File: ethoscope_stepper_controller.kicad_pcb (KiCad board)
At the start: 2 copper layers, 74.9 x 74.9 mm, 63 parts, among them P1 PWR_JACK_2.1x5.5_SMD_VERT, T1 TERM_BLK_HDR_4POS_VERT_0.138IN, T2 TERM_BLK_HDR_4POS_VERT_0.138IN, T3 TERM_BLK_HDR_4POS_VERT_0.138IN, T4 TERM_BLK_HDR_4POS_VERT_0.138IN, T5 TERM_BLK_HDR_4POS_VERT_0.138IN, T6 TERM_BLK_HDR_4POS_VERT_0.138IN, T7 TERM_BLK_HDR_4POS_VERT_0.138IN, U1 TMC429, U10 DRV8846, U2 DRV8846, U3 DRV8846, U4 DRV8846, U5 TMC429, U6 DRV8846, U7 DRV8846, U8 DRV8846, U9 TMC429

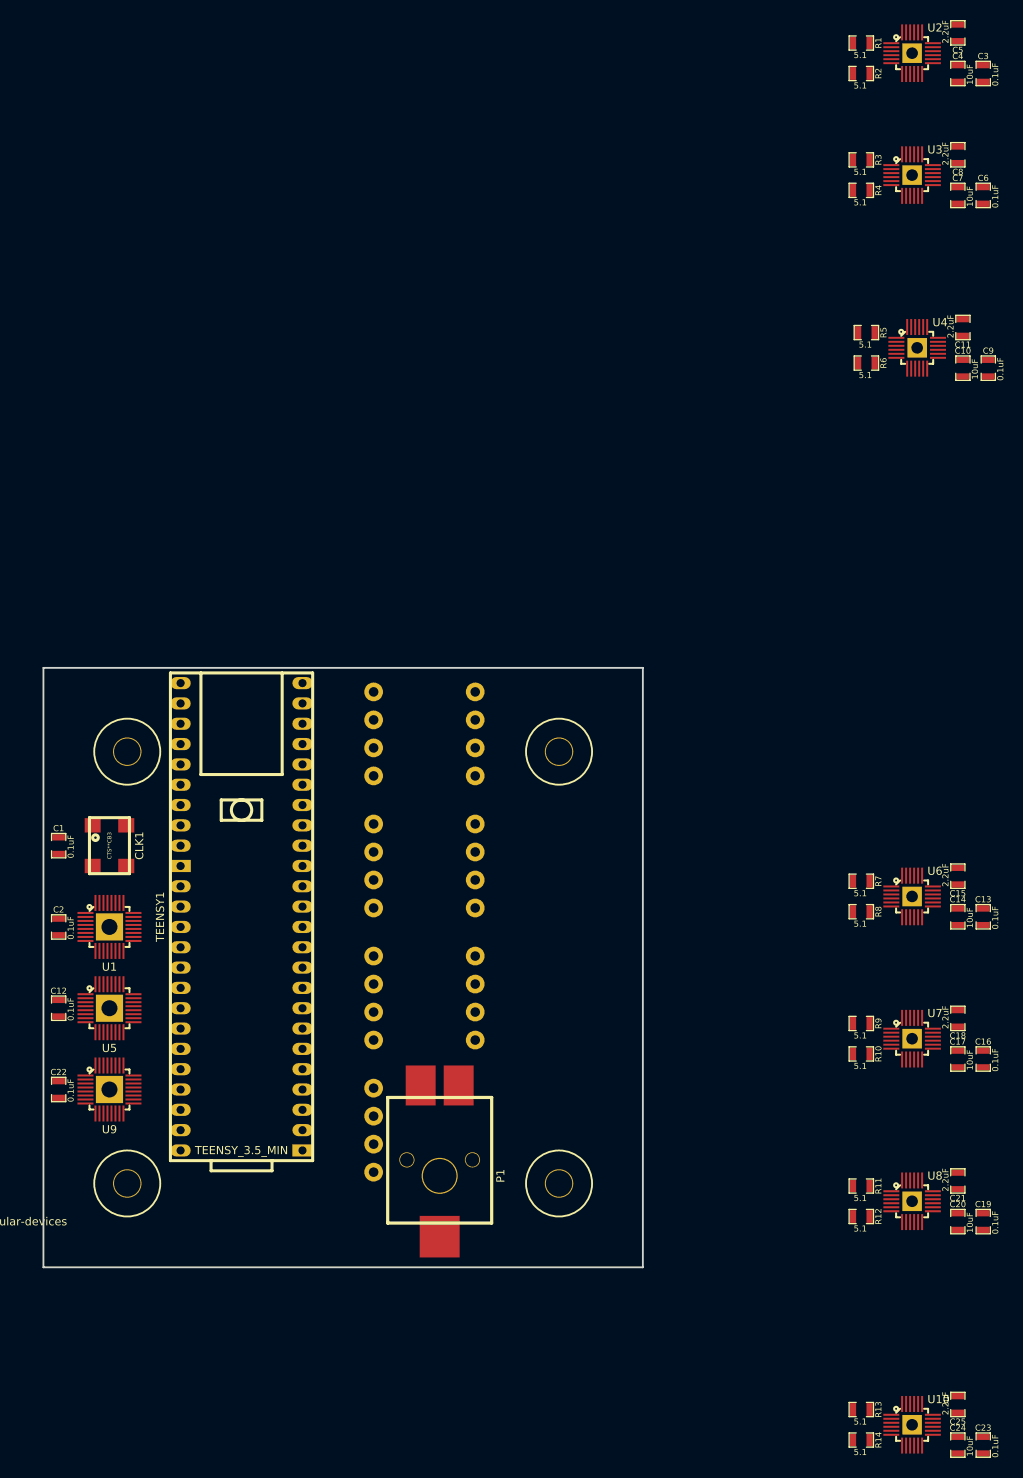
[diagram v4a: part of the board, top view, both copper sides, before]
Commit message: Added a pull-up resistor and tri-state buffer.
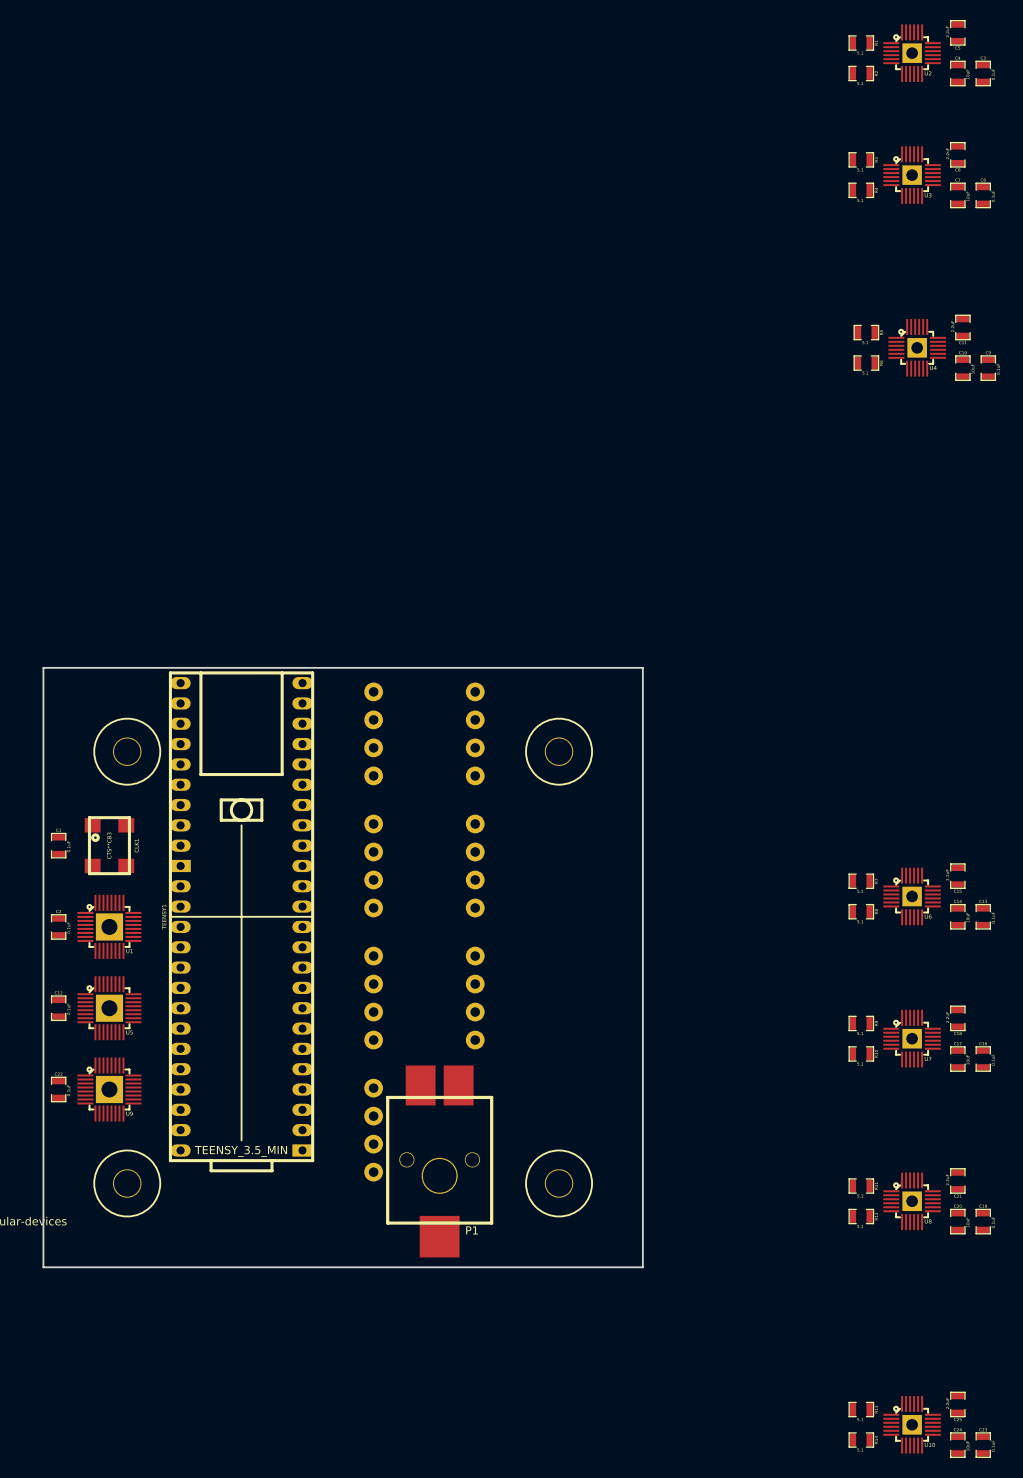
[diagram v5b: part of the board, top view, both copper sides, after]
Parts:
- C10, C11, C14, C15, C17, C18, C20, C21, C24, C25, C4, C5, C7, C8, R1, R10, R11, R12, R13, R14, R2, R3, R4, R5, R6, R7, R8, R9: footprint footprints:SM0805 -> ethoscope_stepper_controller:SM0805

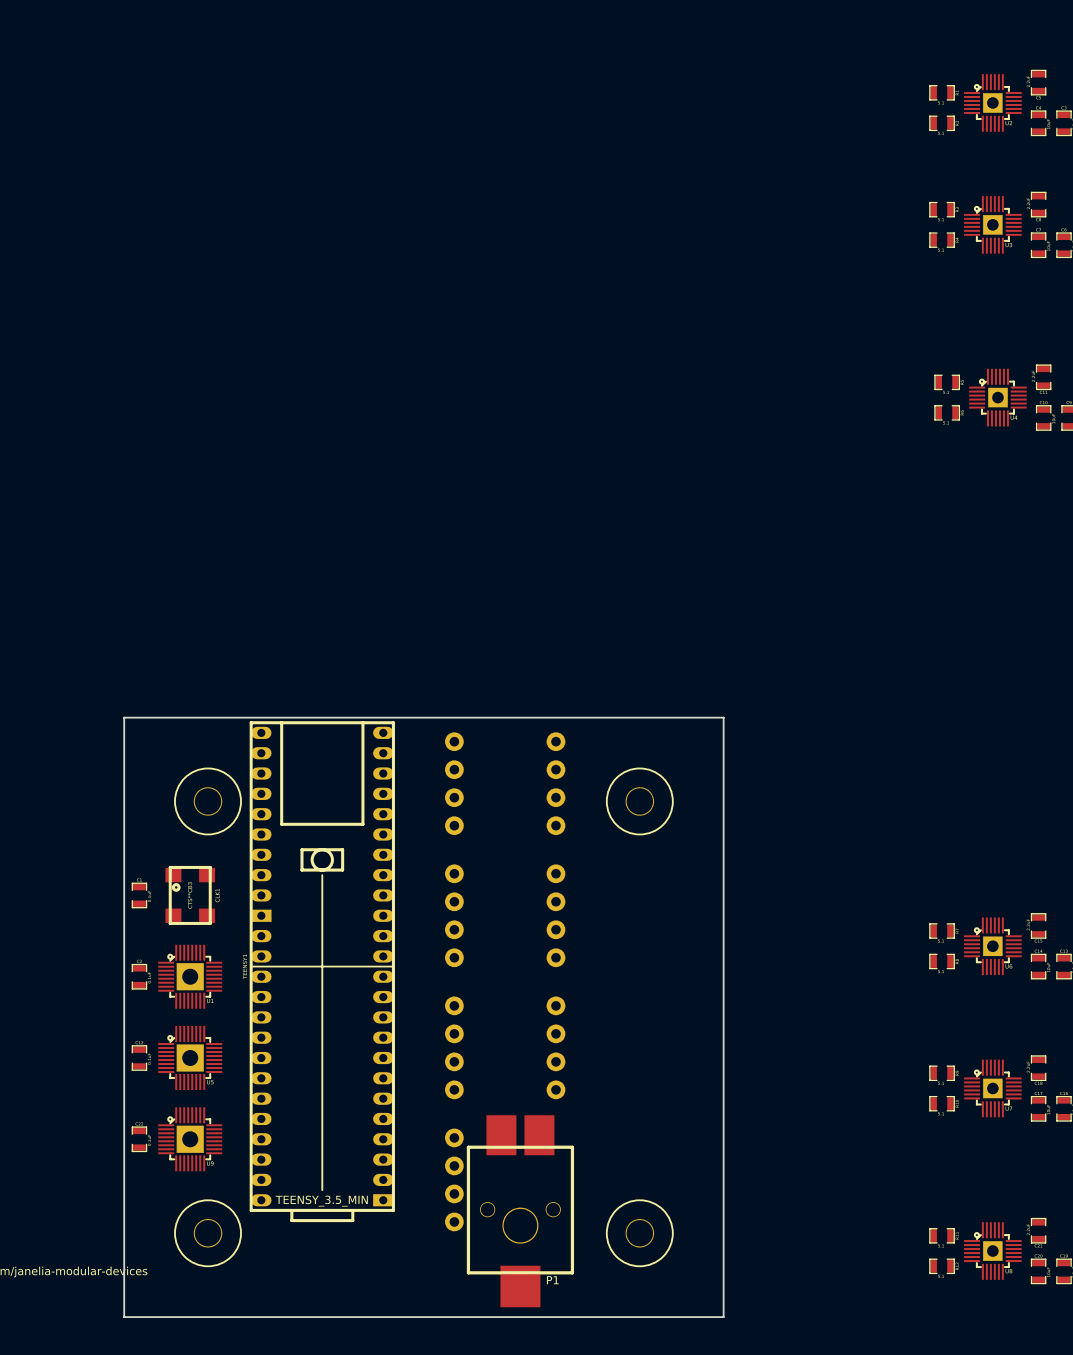
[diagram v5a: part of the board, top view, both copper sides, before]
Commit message: Placed more parts, but saved with errors.
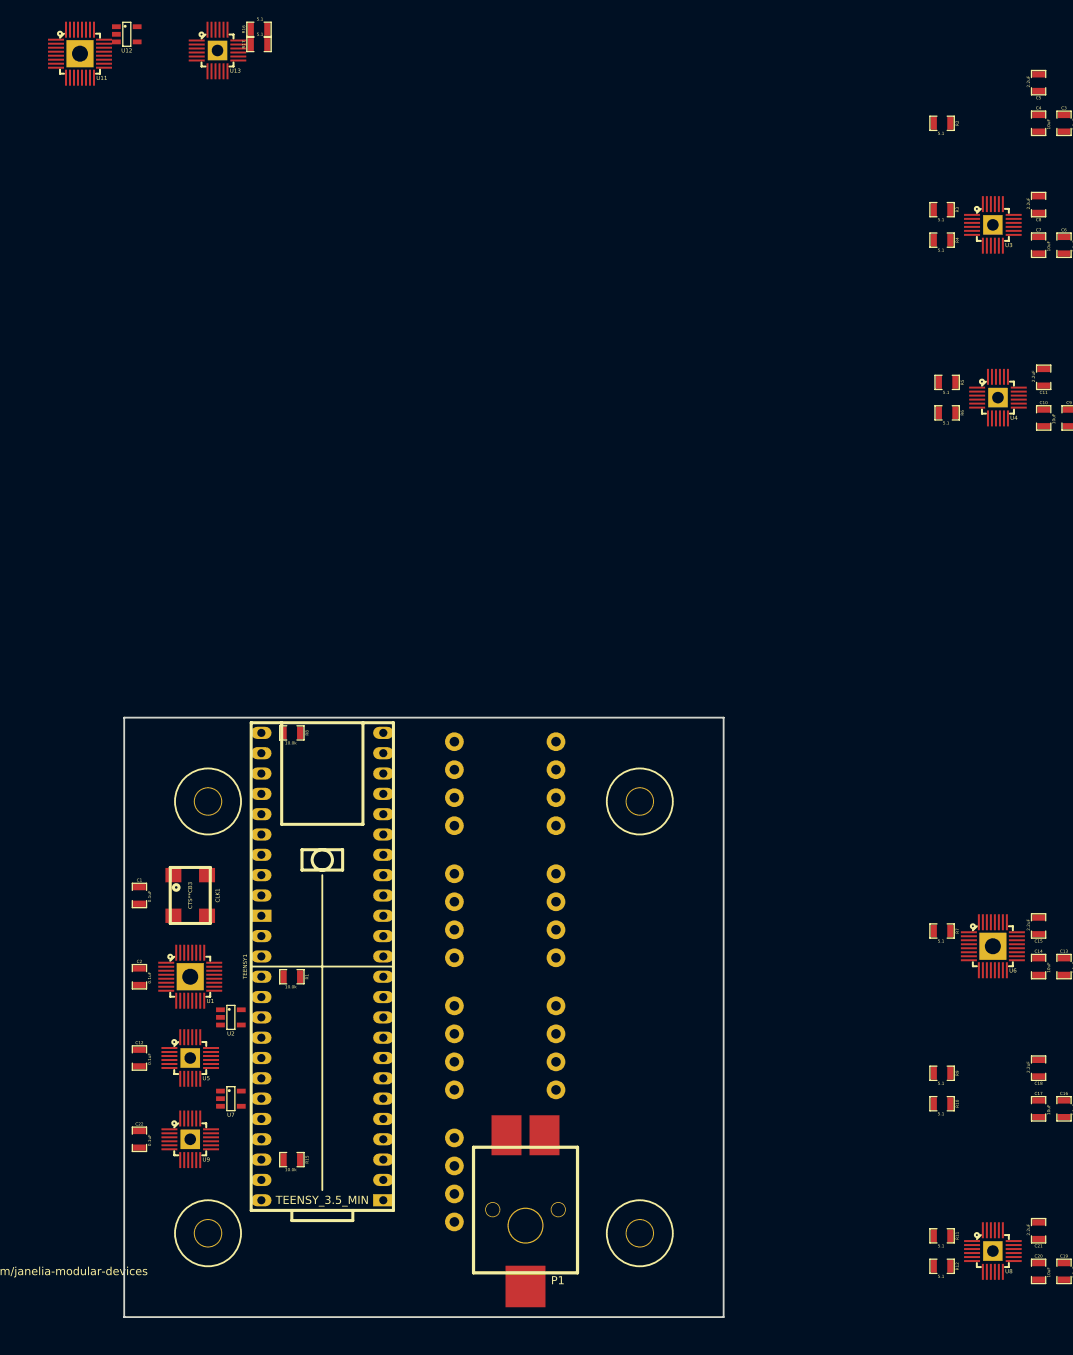
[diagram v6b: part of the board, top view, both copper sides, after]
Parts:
- added R15: 10.0k, ethoscope_stepper_controller:SM0805, F.Cu at (135.9, 119.4)
- added R16: 5.1, ethoscope_stepper_controller:SM0805, F.Cu at (131.8, -21.9)
- added R17: 5.1, ethoscope_stepper_controller:SM0805, F.Cu at (131.8, -20.0)
- added U11: TMC429, ethoscope_stepper_controller:QFN-5x5-32, F.Cu at (109.4, -18.9)
- added U12: BUFFER_TRI_STATE, ethoscope_stepper_controller:SOT-23-5, F.Cu at (115.3, -21.3)
- added U13: DRV8846, ethoscope_stepper_controller:VQFN-4x4-24, F.Cu at (126.6, -19.3)
- R1, R8: value 5.1 -> 10.0k
- U2, U7: value DRV8846 -> BUFFER_TRI_STATE; footprint ethoscope_stepper_controller:VQFN-4x4-24 -> ethoscope_stepper_controller:SOT-23-5
- U5, U9: value TMC429 -> DRV8846; footprint ethoscope_stepper_controller:QFN-5x5-32 -> ethoscope_stepper_controller:VQFN-4x4-24
- U6: value DRV8846 -> TMC429; footprint ethoscope_stepper_controller:VQFN-4x4-24 -> ethoscope_stepper_controller:QFN-5x5-32
- moved U2 148.8 mm to (128.3, 101.6)
- moved R1 137.2 mm to (135.9, 96.5)
- moved U7 95.3 mm to (128.3, 111.8)
- moved R8 86.2 mm to (135.9, 66.0)
- moved P1 0.63 mm to (165.1, 127.6)
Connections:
- R1 pad 1: /tmc429_0/stepper_driver_0/AISEN -> +3V3
- R1 pad 2: GND -> /CS_429_0
- R10 pad 1: /tmc429_1/stepper_driver_1/BISEN -> /tmc429_1/stepper_driver_0/BISEN
- R11 pad 1: /tmc429_1/stepper_driver_2/AISEN -> /tmc429_1/stepper_driver_1/AISEN
- R12 pad 1: /tmc429_1/stepper_driver_2/BISEN -> /tmc429_1/stepper_driver_1/BISEN
- R13 pad 1: /tmc429_2/stepper_driver_0/AISEN -> /tmc429_1/stepper_driver_2/AISEN
- R14 pad 1: /tmc429_2/stepper_driver_0/BISEN -> /tmc429_1/stepper_driver_2/BISEN
- R2 pad 1: /tmc429_0/stepper_driver_0/BISEN -> /tmc429_0/stepper_driver_0/AISEN
- R3 pad 1: /tmc429_0/stepper_driver_1/AISEN -> /tmc429_0/stepper_driver_0/BISEN
- R4 pad 1: /tmc429_0/stepper_driver_1/BISEN -> /tmc429_0/stepper_driver_1/AISEN
- R5 pad 1: /tmc429_0/stepper_driver_2/AISEN -> /tmc429_0/stepper_driver_1/BISEN
- R6 pad 1: /tmc429_0/stepper_driver_2/BISEN -> /tmc429_0/stepper_driver_2/AISEN
- R7 pad 1: /tmc429_1/stepper_driver_0/AISEN -> /tmc429_0/stepper_driver_2/BISEN
- R8 pad 1: /tmc429_1/stepper_driver_0/BISEN -> +3V3
- R8 pad 2: GND -> /CS_429_1
- R9 pad 1: /tmc429_1/stepper_driver_1/AISEN -> /tmc429_1/stepper_driver_0/AISEN
- U1 pad 12: /MISO -> /tmc429_0/MISO_UB
- U10 pad 1: /tmc429_2/stepper_driver_0/A_+ -> /tmc429_1/stepper_driver_2/A_+
- U10 pad 12: /tmc429_2/STEP_0 -> /tmc429_1/STEP_2
- U10 pad 13: /tmc429_2/DIR_0 -> /tmc429_1/DIR_2
- U10 pad 14: /tmc429_2/stepper_driver_0/VINT -> /tmc429_1/stepper_driver_2/VINT
- U10 pad 17: /tmc429_2/stepper_driver_0/VINT -> /tmc429_1/stepper_driver_2/VINT
- U10 pad 19: /tmc429_2/stepper_driver_0/VINT -> /tmc429_1/stepper_driver_2/VINT
- U10 pad 2: /tmc429_2/stepper_driver_0/AISEN -> /tmc429_1/stepper_driver_2/AISEN
- U10 pad 22: /tmc429_2/stepper_driver_0/VINT -> /tmc429_1/stepper_driver_2/VINT
- U10 pad 23: /tmc429_2/stepper_driver_0/VINT -> /tmc429_1/stepper_driver_2/VINT
- U10 pad 24: /tmc429_2/stepper_driver_0/VINT -> /tmc429_1/stepper_driver_2/VINT
- U10 pad 3: /tmc429_2/stepper_driver_0/A_- -> /tmc429_1/stepper_driver_2/A_-
- U10 pad 4: /tmc429_2/stepper_driver_0/B_- -> /tmc429_1/stepper_driver_2/B_-
- U10 pad 5: /tmc429_2/stepper_driver_0/BISEN -> /tmc429_1/stepper_driver_2/BISEN
- U10 pad 6: /tmc429_2/stepper_driver_0/B_+ -> /tmc429_1/stepper_driver_2/B_+
- U10 pad 9: /tmc429_2/stepper_driver_0/VINT -> /tmc429_1/stepper_driver_2/VINT
- U2 pad 1: /tmc429_0/stepper_driver_0/A_+ -> /CS_429_0
- U2 pad 2: /tmc429_0/stepper_driver_0/AISEN -> /tmc429_0/MISO_UB
- U2 pad 3: /tmc429_0/stepper_driver_0/A_- -> GND
- U2 pad 4: /tmc429_0/stepper_driver_0/B_- -> /MISO
- U2 pad 5: /tmc429_0/stepper_driver_0/BISEN -> +3V3
- U3 pad 1: /tmc429_0/stepper_driver_1/A_+ -> /tmc429_0/stepper_driver_0/A_+
- U3 pad 12: /tmc429_0/STEP_1 -> /tmc429_0/STEP_0
- U3 pad 13: /tmc429_0/DIR_1 -> /tmc429_0/DIR_0
- U3 pad 14: /tmc429_0/stepper_driver_1/VINT -> /tmc429_0/stepper_driver_0/VINT
- U3 pad 17: /tmc429_0/stepper_driver_1/VINT -> /tmc429_0/stepper_driver_0/VINT
- U3 pad 19: /tmc429_0/stepper_driver_1/VINT -> /tmc429_0/stepper_driver_0/VINT
- U3 pad 2: /tmc429_0/stepper_driver_1/AISEN -> /tmc429_0/stepper_driver_0/AISEN
- U3 pad 22: /tmc429_0/stepper_driver_1/VINT -> /tmc429_0/stepper_driver_0/VINT
- U3 pad 23: /tmc429_0/stepper_driver_1/VINT -> /tmc429_0/stepper_driver_0/VINT
- U3 pad 24: /tmc429_0/stepper_driver_1/VINT -> /tmc429_0/stepper_driver_0/VINT
- U3 pad 3: /tmc429_0/stepper_driver_1/A_- -> /tmc429_0/stepper_driver_0/A_-
- U3 pad 4: /tmc429_0/stepper_driver_1/B_- -> /tmc429_0/stepper_driver_0/B_-
- U3 pad 5: /tmc429_0/stepper_driver_1/BISEN -> /tmc429_0/stepper_driver_0/BISEN
- U3 pad 6: /tmc429_0/stepper_driver_1/B_+ -> /tmc429_0/stepper_driver_0/B_+
- U3 pad 9: /tmc429_0/stepper_driver_1/VINT -> /tmc429_0/stepper_driver_0/VINT
- U4 pad 1: /tmc429_0/stepper_driver_2/A_+ -> /tmc429_0/stepper_driver_1/A_+
- U4 pad 12: /tmc429_0/STEP_2 -> /tmc429_0/STEP_1
- U4 pad 13: /tmc429_0/DIR_2 -> /tmc429_0/DIR_1
- U4 pad 14: /tmc429_0/stepper_driver_2/VINT -> /tmc429_0/stepper_driver_1/VINT
- U4 pad 17: /tmc429_0/stepper_driver_2/VINT -> /tmc429_0/stepper_driver_1/VINT
- U4 pad 19: /tmc429_0/stepper_driver_2/VINT -> /tmc429_0/stepper_driver_1/VINT
- U4 pad 2: /tmc429_0/stepper_driver_2/AISEN -> /tmc429_0/stepper_driver_1/AISEN
- U4 pad 22: /tmc429_0/stepper_driver_2/VINT -> /tmc429_0/stepper_driver_1/VINT
- U4 pad 23: /tmc429_0/stepper_driver_2/VINT -> /tmc429_0/stepper_driver_1/VINT
- U4 pad 24: /tmc429_0/stepper_driver_2/VINT -> /tmc429_0/stepper_driver_1/VINT
- U4 pad 3: /tmc429_0/stepper_driver_2/A_- -> /tmc429_0/stepper_driver_1/A_-
- U4 pad 4: /tmc429_0/stepper_driver_2/B_- -> /tmc429_0/stepper_driver_1/B_-
- U4 pad 5: /tmc429_0/stepper_driver_2/BISEN -> /tmc429_0/stepper_driver_1/BISEN
- U4 pad 6: /tmc429_0/stepper_driver_2/B_+ -> /tmc429_0/stepper_driver_1/B_+
- U4 pad 9: /tmc429_0/stepper_driver_2/VINT -> /tmc429_0/stepper_driver_1/VINT
- U5 pad 1: GND -> /tmc429_0/stepper_driver_2/A_+
- U5 pad 10: /MOSI -> (no net)
- U5 pad 11: (no net) -> /ENABLE_ALL
- U5 pad 12: /MISO -> /tmc429_0/STEP_2
- U5 pad 13: GND -> /tmc429_0/DIR_2
- U5 pad 14: (no net) -> /tmc429_0/stepper_driver_2/VINT
- U5 pad 15: /tmc429_1/STEP_0 -> VAA
- U5 pad 17: /tmc429_1/DIR_0 -> /tmc429_0/stepper_driver_2/VINT
- U5 pad 18: /tmc429_1/STEP_1 -> GND
- U5 pad 19: /tmc429_1/STEP_2 -> /tmc429_0/stepper_driver_2/VINT
- U5 pad 2: GND -> /tmc429_0/stepper_driver_2/AISEN
- U5 pad 20: /tmc429_1/DIR_2 -> GND
- U5 pad 21: +3V3 -> GND
- U5 pad 22: +3V3 -> /tmc429_0/stepper_driver_2/VINT
- U5 pad 23: GND -> /tmc429_0/stepper_driver_2/VINT
- U5 pad 24: (no net) -> /tmc429_0/stepper_driver_2/VINT
- U5 pad 3: +3V3 -> /tmc429_0/stepper_driver_2/A_-
- U5 pad 4: GND -> /tmc429_0/stepper_driver_2/B_-
- U5 pad 5: /CLK -> /tmc429_0/stepper_driver_2/BISEN
- U5 pad 6: GND -> /tmc429_0/stepper_driver_2/B_+
- U5 pad 7: /CS_429_1 -> (no net)
- U5 pad 8: /SCK -> (no net)
- U5 pad 9: (no net) -> /tmc429_0/stepper_driver_2/VINT
- U6 pad 1: /tmc429_1/stepper_driver_0/A_+ -> GND
- U6 pad 10: (no net) -> /MOSI
- U6 pad 11: /ENABLE_ALL -> (no net)
- U6 pad 12: /tmc429_1/STEP_0 -> /tmc429_1/MISO_UB
- U6 pad 13: /tmc429_1/DIR_0 -> GND
- U6 pad 14: /tmc429_1/stepper_driver_0/VINT -> (no net)
- U6 pad 15: VAA -> /tmc429_1/STEP_0
- U6 pad 17: /tmc429_1/stepper_driver_0/VINT -> /tmc429_1/DIR_0
- U6 pad 18: GND -> /tmc429_1/STEP_1
- U6 pad 19: /tmc429_1/stepper_driver_0/VINT -> /tmc429_1/STEP_2
- U6 pad 2: /tmc429_1/stepper_driver_0/AISEN -> GND
- U6 pad 20: GND -> /tmc429_1/DIR_2
- U6 pad 21: GND -> +3V3
- U6 pad 22: /tmc429_1/stepper_driver_0/VINT -> +3V3
- U6 pad 23: /tmc429_1/stepper_driver_0/VINT -> GND
- U6 pad 24: /tmc429_1/stepper_driver_0/VINT -> (no net)
- U6 pad 3: /tmc429_1/stepper_driver_0/A_- -> +3V3
- U6 pad 4: /tmc429_1/stepper_driver_0/B_- -> GND
- U6 pad 5: /tmc429_1/stepper_driver_0/BISEN -> /CLK
- U6 pad 6: /tmc429_1/stepper_driver_0/B_+ -> GND
- U6 pad 7: (no net) -> /CS_429_1
- U6 pad 8: (no net) -> /SCK
- U6 pad 9: /tmc429_1/stepper_driver_0/VINT -> (no net)
- U7 pad 1: /tmc429_1/stepper_driver_1/A_+ -> /CS_429_1
- U7 pad 2: /tmc429_1/stepper_driver_1/AISEN -> /tmc429_1/MISO_UB
- U7 pad 3: /tmc429_1/stepper_driver_1/A_- -> GND
- U7 pad 4: /tmc429_1/stepper_driver_1/B_- -> /MISO
- U7 pad 5: /tmc429_1/stepper_driver_1/BISEN -> +3V3
- U8 pad 1: /tmc429_1/stepper_driver_2/A_+ -> /tmc429_1/stepper_driver_0/A_+
- U8 pad 12: /tmc429_1/STEP_2 -> /tmc429_1/STEP_0
- U8 pad 13: /tmc429_1/DIR_2 -> /tmc429_1/DIR_0
- U8 pad 14: /tmc429_1/stepper_driver_2/VINT -> /tmc429_1/stepper_driver_0/VINT
- U8 pad 17: /tmc429_1/stepper_driver_2/VINT -> /tmc429_1/stepper_driver_0/VINT
- U8 pad 19: /tmc429_1/stepper_driver_2/VINT -> /tmc429_1/stepper_driver_0/VINT
- U8 pad 2: /tmc429_1/stepper_driver_2/AISEN -> /tmc429_1/stepper_driver_0/AISEN
- U8 pad 22: /tmc429_1/stepper_driver_2/VINT -> /tmc429_1/stepper_driver_0/VINT
- U8 pad 23: /tmc429_1/stepper_driver_2/VINT -> /tmc429_1/stepper_driver_0/VINT
- U8 pad 24: /tmc429_1/stepper_driver_2/VINT -> /tmc429_1/stepper_driver_0/VINT
- U8 pad 3: /tmc429_1/stepper_driver_2/A_- -> /tmc429_1/stepper_driver_0/A_-
- U8 pad 4: /tmc429_1/stepper_driver_2/B_- -> /tmc429_1/stepper_driver_0/B_-
- U8 pad 5: /tmc429_1/stepper_driver_2/BISEN -> /tmc429_1/stepper_driver_0/BISEN
- U8 pad 6: /tmc429_1/stepper_driver_2/B_+ -> /tmc429_1/stepper_driver_0/B_+
- U8 pad 9: /tmc429_1/stepper_driver_2/VINT -> /tmc429_1/stepper_driver_0/VINT
- U9 pad 1: GND -> /tmc429_1/stepper_driver_1/A_+
- U9 pad 10: /MOSI -> (no net)
- U9 pad 11: (no net) -> /ENABLE_ALL
- U9 pad 12: /MISO -> /tmc429_1/STEP_1
- U9 pad 13: GND -> /tmc429_1/DIR_1
- U9 pad 14: (no net) -> /tmc429_1/stepper_driver_1/VINT
- U9 pad 15: /tmc429_2/STEP_0 -> VAA
- U9 pad 17: /tmc429_2/DIR_0 -> /tmc429_1/stepper_driver_1/VINT
- U9 pad 18: (no net) -> GND
- U9 pad 19: (no net) -> /tmc429_1/stepper_driver_1/VINT
- U9 pad 2: GND -> /tmc429_1/stepper_driver_1/AISEN
- U9 pad 20: (no net) -> GND
- U9 pad 21: +3V3 -> GND
- U9 pad 22: +3V3 -> /tmc429_1/stepper_driver_1/VINT
- U9 pad 23: GND -> /tmc429_1/stepper_driver_1/VINT
- U9 pad 24: (no net) -> /tmc429_1/stepper_driver_1/VINT
- U9 pad 3: +3V3 -> /tmc429_1/stepper_driver_1/A_-
- U9 pad 4: GND -> /tmc429_1/stepper_driver_1/B_-
- U9 pad 5: /CLK -> /tmc429_1/stepper_driver_1/BISEN
- U9 pad 6: GND -> /tmc429_1/stepper_driver_1/B_+
- U9 pad 7: /CS_429_2 -> (no net)
- U9 pad 8: /SCK -> (no net)
- U9 pad 9: (no net) -> /tmc429_1/stepper_driver_1/VINT

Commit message: Initial part placement.
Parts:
- T1, T2, T3, T4, T5, T6, T7: value TERM_BLK_HDR_4POS_VERT_0.138IN -> TERM_BLK
- moved U12 143.8 mm to (128.3, 121.9)
- moved U13 137.8 mm to (185.4, 105.4), turned to 270 degrees
- moved U11 136.4 mm to (123.2, 116.8)
- moved R16 133.4 mm to (186.7, 99.7), turned to 90 degrees
- moved R17 130.7 mm to (184.2, 99.7), turned to 90 degrees
- moved C3 115.2 mm to (160.0, 79.5), turned to 180 degrees
- moved C5 112.7 mm to (165.1, 77.5), turned to 0 degrees
- moved C4 111.7 mm to (160.0, 77.5), turned to 180 degrees
- moved C6 103.5 mm to (182.9, 96.0), turned to 180 degrees
- moved C8 102.6 mm to (188.0, 94.0), turned to 0 degrees
- moved U6 101.3 mm to (123.2, 106.7)
- moved C9 100.7 mm to (160.0, 96.0), turned to 180 degrees
- moved C7 100.3 mm to (182.9, 94.0), turned to 180 degrees
- moved C11 97.1 mm to (165.1, 94.0), turned to 0 degrees
- moved C10 97.0 mm to (160.0, 94.0), turned to 180 degrees
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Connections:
- U11 pad 12: /MISO -> /tmc429_2/MISO_UB
- U12 pad 2: /MISO -> /tmc429_2/MISO_UB
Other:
- net class Default: clearance 0.0254 -> 0.1016; via_dia 0.889 -> 0.508; via_drill 0.635 -> 0.254
- net class GND: trace_width 0.4064 -> 0.254; via_dia 0.889 -> 0.508; via_drill 0.635 -> 0.254
- net class LEDPOWER: clearance 0.254 -> 0.1016; trace_width 0.6096 -> 0.254; via_dia 0.889 -> 0.508; via_drill 0.635 -> 0.254
- net class POWER: clearance 0.254 -> 0.1016; trace_width 0.8128 -> 0.254; via_dia 0.889 -> 0.508; via_drill 0.635 -> 0.254
- net class SIGNAL: trace_width 0.4064 -> 0.254; via_dia 0.889 -> 0.508; via_drill 0.635 -> 0.254
- net class SUPERPOWER: clearance 0.254 -> 0.1016; trace_width 1.2192 -> 0.254; via_dia 0.889 -> 0.508; via_drill 0.635 -> 0.254
- rule trace_clearance: 0.0254 -> 0.1016
- rule trace_min: 0.254 -> 0.2032
- rule via_min_drill: 0.508 -> 0.254
- rule via_min_size: 0.889 -> 0.508
